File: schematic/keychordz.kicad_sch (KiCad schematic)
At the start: 54 parts, among them IC1 MCP73833-BZI_UN, J1 USB_C_Receptacle_USB2.0, J2 Conn_01x04_Male, SW1 SW_Push, SW2 SW_Push, SW3 SW_Push, SW4 SW_Push, SW5 SW_Push, SW6 SW_Push, SW7 SW_Push, SW8 SW_Push, U1 nRF52840, X1 32MHz, X2 32.768kHz

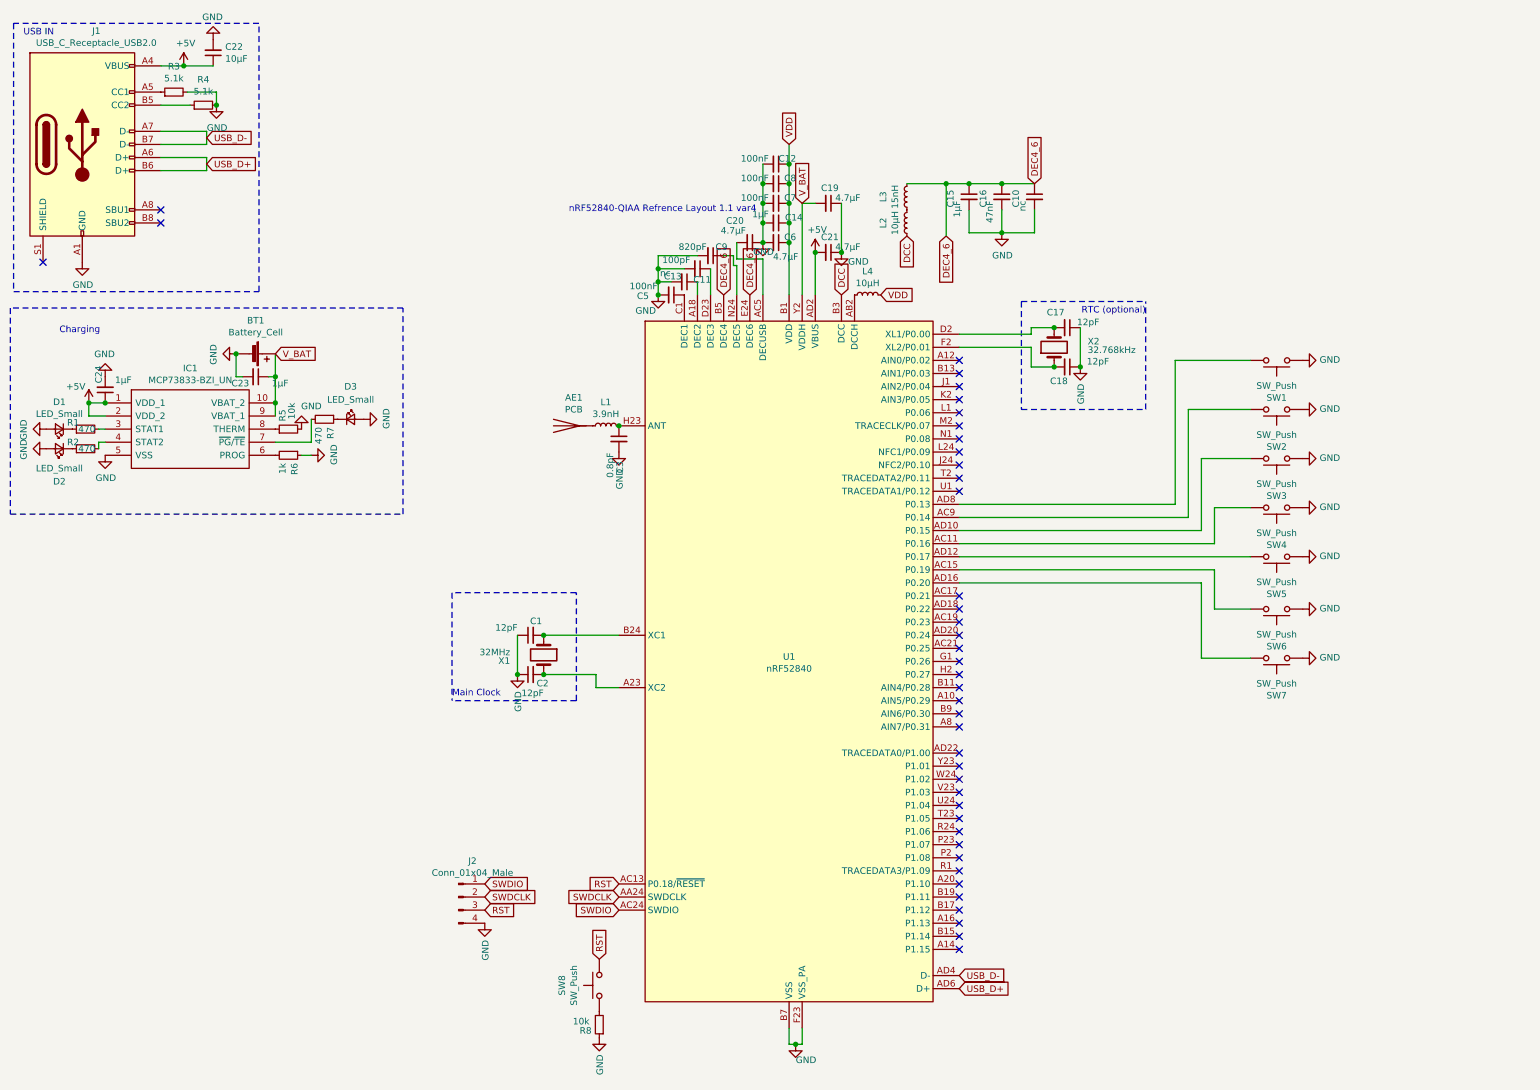
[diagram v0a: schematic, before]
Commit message: add Breakout
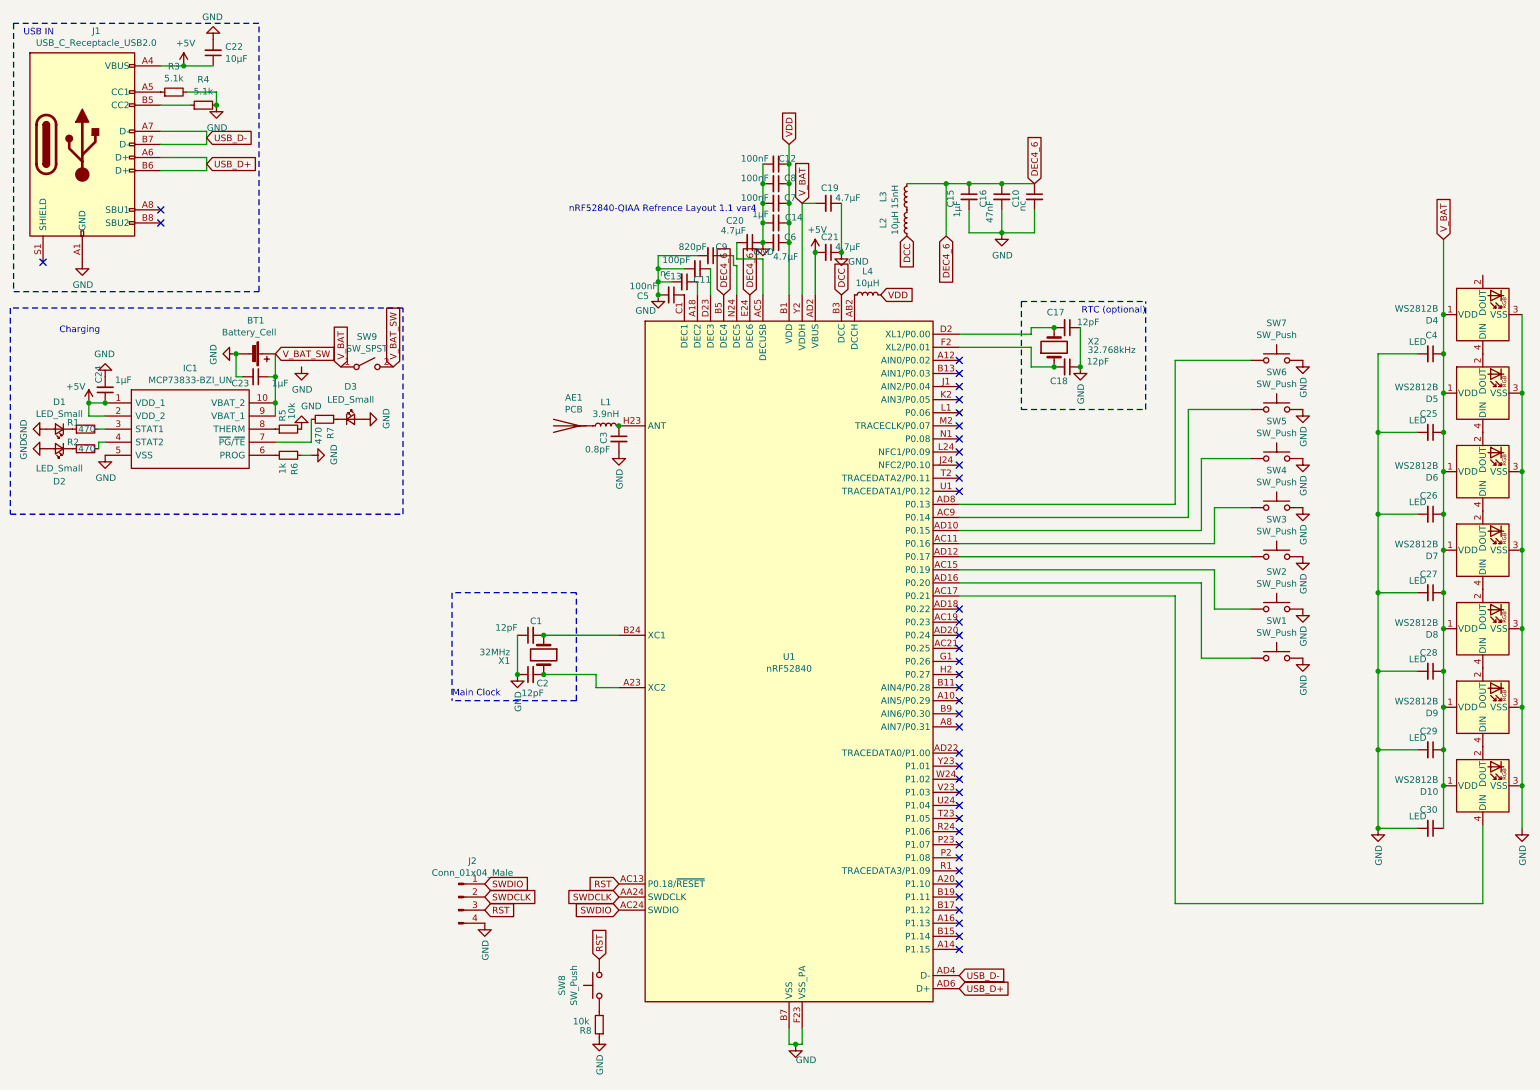
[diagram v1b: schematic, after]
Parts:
- added C25, C26, C27, C28, C29, C30, C4: LED, Capacitor_SMD:C_0603_1608Metric_Pad1.08x0.95mm_HandSolder, symbol Device:C_Small
- added D10, D4, D5, D6, D7, D8, D9: WS2812B, LED_SMD:LED_WS2812B_PLCC4_2.2x2.2mm, symbol LED:WS2812B
- added SW9: SW_SPST, Button_Switch_THT:SW_DIP_SPSTx02_Slide_6.7x6.64mm_W7.62mm_P2.54mm_LowProfile, symbol Switch:SW_SPST
- AE1: footprint RF_Antenna:Texas_SWRA117D_2.4GHz_Left -> RF_Antenna:Texas_SWRA117D_2.4GHz_Right
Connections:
- net GND: now also SW1.2, SW2.2, SW3.2, SW4.2, SW5.2, SW6.2, SW7.2, C25.2, C26.2, C27.2, C28.2, C29.2, C30.2, C4.2, D10.3 (VSS), D4.3 (VSS), D5.3 (VSS), D6.3 (VSS), D7.3 (VSS), D8.3 (VSS), D9.3 (VSS); no longer SW1.1, SW2.1, SW3.1, SW4.1, SW5.1, SW6.1, SW7.1
- net V_BAT: now also C25.1, C26.1, C27.1, C28.1, C29.1, C30.1, C4.1, D10.1 (VDD), D4.1 (VDD), D5.1 (VDD), D6.1 (VDD), D7.1 (VDD), D8.1 (VDD), D9.1 (VDD), SW9.1 (A); no longer BT1.1 (+), C23.1, IC1.10 (VBAT_2), IC1.9 (VBAT_1)
- net at U1.AD12 (P0.17): now also SW3.1; no longer SW5.2
- net at U1.AC11 (P0.16): now also SW4.1; no longer SW4.2
- net at U1.AD10 (P0.15): now also SW5.1; no longer SW3.2
- net at U1.AC9 (P0.14): now also SW6.1; no longer SW2.2
- net at U1.AD8 (P0.13): now also SW7.1; no longer SW1.2
- net at U1.AC15 (P0.19): now also SW2.1; no longer SW6.2
- net at U1.AC17 (P0.21): now also D10.4 (DIN)
- net at U1.AD16 (P0.20): now also SW1.1; no longer SW7.2
- new net: D6.4 (DIN), D7.2 (DOUT)
- new net: D7.4 (DIN), D8.2 (DOUT)
- new net: D8.4 (DIN), D9.2 (DOUT)
- new net: D5.4 (DIN), D6.2 (DOUT)
- new net: D10.2 (DOUT), D9.4 (DIN)
- new net: D4.4 (DIN), D5.2 (DOUT)
- new net V_BAT_SW: BT1.1 (+), C23.1, IC1.10 (VBAT_2), IC1.9 (VBAT_1), SW9.2 (B)
- no-connect marks 41 -> 40
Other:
- moved on the sheet: SW1, SW2, SW3, SW4, SW5, SW6, SW7

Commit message: keyboard schematic with breakout
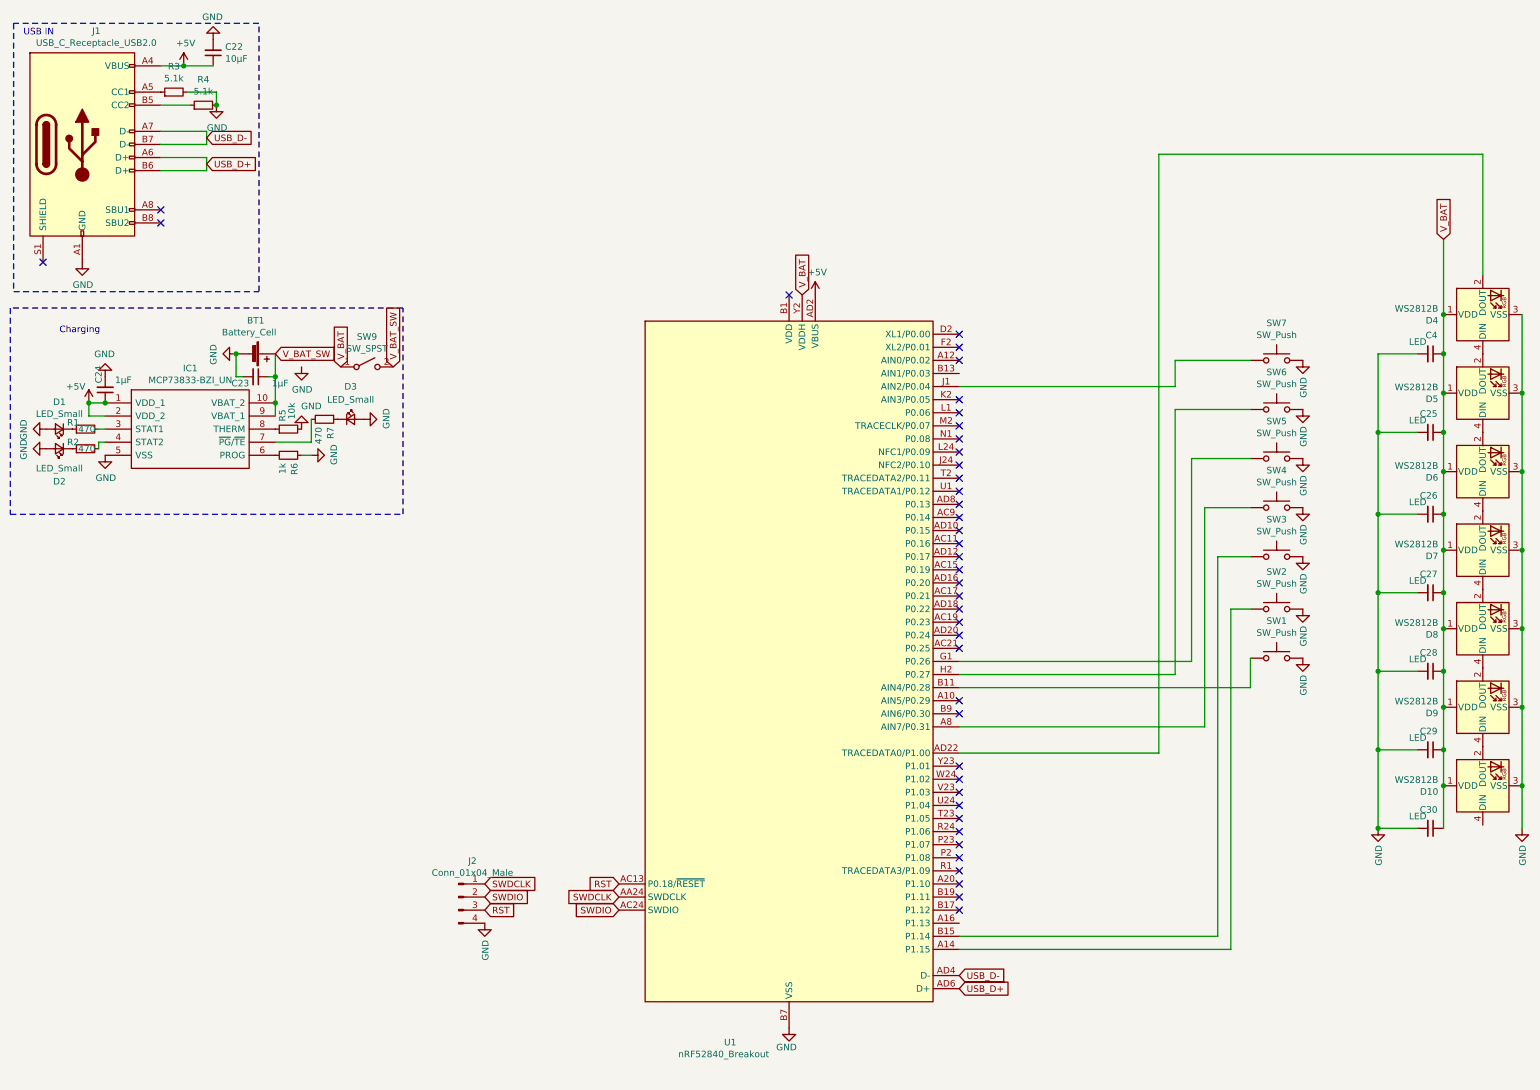
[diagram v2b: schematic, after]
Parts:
- removed AE1: PCB, RF_Antenna:Texas_SWRA117D_2.4GHz_Right, symbol Device:Antenna
- removed C1, C17, C18, C2: 12pF, Capacitor_SMD:C_0402_1005Metric_Pad0.74x0.62mm_HandSolder, symbol Device:C_Small
- removed C10, C13: nc, Capacitor_SMD:C_0402_1005Metric_Pad0.74x0.62mm_HandSolder, symbol Device:C_Small
- removed C11: 100pF, Capacitor_SMD:C_0603_1608Metric_Pad1.08x0.95mm_HandSolder, symbol Device:C_Small
- removed C12, C5, C7, C8: 100nF, Capacitor_SMD:C_0402_1005Metric_Pad0.74x0.62mm_HandSolder, symbol Device:C_Small
- removed C14, C15: 1µF, Capacitor_SMD:C_0603_1608Metric_Pad1.08x0.95mm_HandSolder, symbol Device:C_Small
- removed C16: 47nF, Capacitor_SMD:C_0402_1005Metric_Pad0.74x0.62mm_HandSolder, symbol Device:C_Small
- removed C19, C21: 4.7µF, Capacitor_SMD:C_0603_1608Metric_Pad1.08x0.95mm_HandSolder, symbol Device:C_Small
- removed C20, C6: 4.7µF, Capacitor_SMD:C_1206_3216Metric_Pad1.33x1.80mm_HandSolder, symbol Device:C_Small
- removed C3: 0.8pF, Capacitor_SMD:C_0201_0603Metric_Pad0.64x0.40mm_HandSolder, symbol Device:C_Small
- removed C9: 820pF, Capacitor_SMD:C_0402_1005Metric_Pad0.74x0.62mm_HandSolder, symbol Device:C_Small
- removed L1: 3.9nH, Inductor_SMD:L_0402_1005Metric_Pad0.77x0.64mm_HandSolder, symbol Device:L_Small
- removed L2, L4: 10µH, Inductor_SMD:L_1210_3225Metric_Pad1.42x2.65mm_HandSolder, symbol Device:L_Small
- removed L3: 15nH, Inductor_SMD:L_0402_1005Metric_Pad0.77x0.64mm_HandSolder, symbol Device:L_Small
- removed R8: 10k, Resistor_SMD:R_0402_1005Metric_Pad0.72x0.64mm_HandSolder, symbol Device:R_Small
- removed SW8: SW_Push, Button_Switch_SMD:SW_SPST_PTS636, symbol Switch:SW_Push
- removed U1: nRF52840, Package_DFN_QFN:Nordic_AQFN-73-1EP_7x7mm_P0.5mm, symbol MCU_Nordic:nRF52840
- removed X1: 32MHz, Crystal:Crystal_SMD_2016-4Pin_2.0x1.6mm, symbol Device:Crystal
- removed X2: 32.768kHz, Crystal:Crystal_SMD_MicroCrystal_CC7V-T1A-2Pin_3.2x1.5mm_HandSoldering, symbol Device:Crystal
- added U1: nRF52840_Breakout, schematic:nRF52840_Breakout, symbol MCU_Nordic:nRF52840_Breakout
- J1: footprint Connector_USB:USB_C_Receptacle_Amphenol_12401610E4-2A -> Connector_USB:USB_C_Receptacle_Amphenol_12401548E4-2A
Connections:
- net +5V: now also U1.AD2 (VBUS)
- net GND: now also U1.B7 (VSS)
- net RST: now also U1.AC13 (P0.18/~RESET)
- net SWDCLK: now also J2.1 (Pin_1), U1.AA24 (SWDCLK); no longer J2.2 (Pin_2)
- net SWDIO: now also J2.2 (Pin_2), U1.AC24 (SWDIO); no longer J2.1 (Pin_1)
- net USB_D+: now also U1.AD6 (D+)
- net USB_D-: now also U1.AD4 (D-)
- net V_BAT: now also U1.Y2 (VDDH)
- net at SW5.1: now also U1.G1 (P0.26)
- net at SW4.1: now also U1.A8 (AIN7/P0.31)
- net at SW3.1: now also U1.B15 (P1.14)
- net at SW2.1: now also U1.A14 (P1.15)
- net at SW1.1: now also U1.B11 (AIN4/P0.28)
- net at SW6.1: now also U1.H2 (P0.27)
- net at SW7.1: now also U1.J1 (AIN2/P0.04)
- net at D4.2 (DOUT): now also U1.AD22 (TRACEDATA0/P1.00)
- no-connect marks 40 -> 41
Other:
- note removed: "Main Clock"
- note removed: "RTC (optional)"
- note removed: "nRF52840-QIAA Refrence Layout 1.1 var4"
